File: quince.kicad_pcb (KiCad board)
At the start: 2 copper layers, 70.7 x 53.3 mm, 26 parts, among them J1 NEIGHBOR1, J2 NEIGHBOR2, J7 BONUS_ROW, P9 BASEBAND, U1 TLV3502

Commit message: complete layout
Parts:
- removed P9: BASEBAND, gsg-modules:HEADER-2x8
- added C10: 100pF, gsg-modules:0402, F.Cu at (155.6, 91.8)
- added C11: 100nF, gsg-modules:0402, F.Cu at (151.8, 91.3)
- added C12: 100nF, gsg-modules:0402, F.Cu at (158.7, 87.3)
- added C13: 100nF, gsg-modules:0402, F.Cu at (158.3, 90.2)
- added C14: 100pF, gsg-modules:0402, F.Cu at (145.6, 87.8)
- added C15: 100pF, gsg-modules:0402, F.Cu at (145.6, 85.7)
- added C16: 100pF, gsg-modules:0402, F.Cu at (143.9, 86.2)
- added C17: 100pF, gsg-modules:0402, F.Cu at (143.9, 87.3)
- added C18: 270pF, gsg-modules:0402, F.Cu at (139.7, 83.5)
- added C19: 100nF, gsg-modules:0402, F.Cu at (158.7, 86.2)
- added C2: 1nF, gsg-modules:0402, F.Cu at (158.3, 93.8)
- added C20: 100nF, gsg-modules:0402, F.Cu at (156.8, 82.2)
- added C21: 18pF, gsg-modules:0402, F.Cu at (150.8, 80.8)
- added C22: 68pF, gsg-modules:0402, F.Cu at (149.8, 80.8)
- added C23: 68pF, gsg-modules:0402, F.Cu at (148.8, 80.8)
- added C24: 18pF, gsg-modules:0402, F.Cu at (146.8, 80.8)
- added C25: 100nF, gsg-modules:0402, F.Cu at (141.8, 89.5)
- added C26: 8.2nF, gsg-modules:0402, F.Cu at (141.2, 92.0)
- added C27: 100nF, gsg-modules:0402, F.Cu at (141.3, 84.5)
- added C28: 560pF, gsg-modules:0402, F.Cu at (141.2, 90.8)
- added C29: 10nF, gsg-modules:0402, F.Cu at (136.2, 83.2)
- added C3: 18pF, gsg-modules:0402, F.Cu at (152.2, 93.8)
- added C30: 100nF, gsg-modules:0402, F.Cu at (136.7, 91.5)
- added C31: 100nF, gsg-modules:0402, F.Cu at (157.2, 92.2)
- added C32: 100pF, gsg-modules:0402, F.Cu at (157.2, 91.2)
- added C33: 100nF, gsg-modules:0402, F.Cu at (145.2, 90.0)
- added C34: 100pF, gsg-modules:0402, F.Cu at (146.8, 90.0)
- added C35: 100nF, gsg-modules:0402, F.Cu at (153.8, 80.7)
- added C36: 100pF, gsg-modules:0402, F.Cu at (152.8, 81.8)
- added C37: 10uF, gsg-modules:0805, F.Cu at (133.2, 85.1)
- added C38: C, gsg-modules:0402, F.Cu at (131.4, 87.8)
- added C39: 1nF, gsg-modules:0402, F.Cu at (131.4, 91.8)
- added C4: 68pF, gsg-modules:0402, F.Cu at (151.2, 93.8)
- added C40: 1nF, gsg-modules:0402, F.Cu at (131.4, 89.8)
- added C41: 100nF, gsg-modules:0402, F.Cu at (130.2, 97.2)
- added C42: C, gsg-modules:0402, F.Cu at (131.4, 88.8)
- added C5: 68pF, gsg-modules:0402, F.Cu at (150.2, 93.8)
- added C6: 18pF, gsg-modules:0402, F.Cu at (148.2, 93.8)
- added C7: 1nF, gsg-modules:0402, F.Cu at (164.2, 95.2)
- added C8: 100pF, gsg-modules:0402, F.Cu at (154.6, 91.8)
- added C9: 100pF, gsg-modules:0402, F.Cu at (170.6, 95.2)
- added D1: D_TVS, gsg-modules:0402, F.Cu at (172.2, 94.7)
- added FB1: Ferrite_Bead, gsg-modules:0805, F.Cu at (121.5, 113.0)
- added J10: Conn_01x01, gsg-modules:TESTPOINT-50MIL, F.Cu at (146.6, 97.8)
- added J11: Conn_01x01, gsg-modules:TESTPOINT-50MIL, F.Cu at (143.3, 79.3)
- added J12: Conn_01x01, gsg-modules:TESTPOINT-50MIL, F.Cu at (158.4, 88.8)
- added J13: Conn_01x01, gsg-modules:TESTPOINT-50MIL, F.Cu at (158.4, 84.7)
- added J14: Conn_01x01, gsg-modules:TESTPOINT-50MIL, F.Cu at (160.7, 82.8)
- added J15: Conn_01x01, gsg-modules:TESTPOINT-50MIL, F.Cu at (119.2, 111.8)
- added J16: Conn_01x01, gsg-modules:TESTPOINT-50MIL, F.Cu at (134.7, 90.8)
- added J17: Conn_01x01, gsg-modules:TESTPOINT-50MIL, F.Cu at (122.0, 79.7)
- added J18: Conn_01x01, gsg-modules:TESTPOINT-50MIL, F.Cu at (137.1, 92.8)
- added J19: GND, gsg-modules:HEADER-1x2, F.Cu at (161.4, 103.3)
- added J20: Conn_01x01, gsg-modules:TESTPOINT-50MIL, F.Cu at (133.3, 88.0)
- added J21: Conn_01x01, gsg-modules:TESTPOINT-50MIL, F.Cu at (141.1, 82.5)
- added J3: RFIN, gsg-modules:SMA-EDGE, F.Cu at (177.6, 95.2)
- added J4: Conn_01x01, gsg-modules:TESTPOINT-50MIL, F.Cu at (149.2, 96.8)
- added J5: Conn_01x01, gsg-modules:TESTPOINT-50MIL, B.Cu at (150.8, 86.8)
- added J6: Conn_01x01, gsg-modules:TESTPOINT-50MIL, F.Cu at (157.3, 78.7)
- added J8: LO, gsg-modules:SMA-VERTICAL, F.Cu at (139.6, 98.2)
- added J9: Conn_01x01, gsg-modules:TESTPOINT-50MIL, F.Cu at (155.2, 80.8)
- added L1: 470nH, gsg-modules:0402, F.Cu at (151.7, 95.3)
- added L2: 680nH, gsg-modules:0402, F.Cu at (149.7, 95.3)
- added L3: 470nH, gsg-modules:0402, F.Cu at (149.2, 93.8)
- added L4: 3.6nH, gsg-modules:0402, F.Cu at (162.2, 95.2)
- added L5: 470nH, gsg-modules:0402, F.Cu at (150.3, 79.2)
- added L6: 680nH, gsg-modules:0402, F.Cu at (148.3, 79.2)
- added L7: 470nH, gsg-modules:0402, F.Cu at (147.8, 80.8)
- added R17: 0, gsg-modules:0402, F.Cu at (156.8, 80.5)
- added R18: 0, gsg-modules:0402, F.Cu at (154.7, 82.2)
- added R19: 0, gsg-modules:0402, F.Cu at (151.3, 82.2)
- added R20: 100, gsg-modules:0402, F.Cu at (151.8, 80.8)
- added R21: 0, gsg-modules:0402, F.Cu at (157.9, 80.5)
- added R22: 2k2, gsg-modules:0402, F.Cu at (144.8, 80.8)
- added R23: 10k, gsg-modules:0402, F.Cu at (159.8, 80.0)
- added R24: 51, gsg-modules:0402, F.Cu at (142.3, 85.7)
- added R25: 100, gsg-modules:0402, F.Cu at (145.8, 80.8)
- added R26: 3k3, gsg-modules:0402, F.Cu at (145.3, 79.2)
- added R27: 3k, gsg-modules:0402, F.Cu at (139.7, 91.4)
- added R28: 51, gsg-modules:0402, F.Cu at (142.3, 88.0)
- added R29: 1.5k, gsg-modules:0402, F.Cu at (142.7, 91.5)
- added R30: 0, gsg-modules:0402, F.Cu at (139.1, 93.2)
- added R31: 3k3, gsg-modules:0402, F.Cu at (134.8, 84.2)
- added R32: 0, gsg-modules:0402, F.Cu at (132.8, 99.3)
- added R33: 51, gsg-modules:0402, F.Cu at (131.4, 90.8)
- added U2: AD8347, gsg-modules:TSSOP28, F.Cu at (152.3, 86.8)
- added U3: SAW FILTER, gsg-modules:B9413, F.Cu at (157.2, 95.7)
- added U4: LNA, gsg-modules:BGA7H1N6, F.Cu at (160.1, 95.2)
- added U5: BAND PASS FILTER, gsg-modules:2450BP39D100C, F.Cu at (167.3, 95.2)
- added U6: ADF4360, gsg-modules:QFN24-4, F.Cu at (137.7, 87.5)
- added X1: TCXO, gsg-modules:XTAL5.0x3.2mm, F.Cu at (133.1, 95.7)
- C1: value C -> 100nF; footprint gsg-modules:0603 -> gsg-modules:0402
- R1, R2, R3, R4, R5, R6: footprint gsg-modules:0603 -> gsg-modules:0402
- R10, R16: value R -> 200; footprint gsg-modules:0603 -> gsg-modules:0402
- R11, R7: value R -> 100; footprint gsg-modules:0603 -> gsg-modules:0402
- R12, R13, R14: value R -> 0; footprint gsg-modules:0603 -> gsg-modules:0402
- R15: value R -> 10k; footprint gsg-modules:0603 -> gsg-modules:0402
- R8: value R -> 3k3; footprint gsg-modules:0603 -> gsg-modules:0402
- R9: value R -> 2k2; footprint gsg-modules:0603 -> gsg-modules:0402
- moved R6 46.1 mm to (120.8, 94.9), turned to 90 degrees
- moved R5 44.6 mm to (122.3, 94.9), turned to 90 degrees
- moved R3 39.9 mm to (127.1, 101.6)
- moved R4 39.9 mm to (127.1, 100.1)
- moved U1 31.3 mm to (122.9, 100.8), turned to 270 degrees
- moved R2 26.6 mm to (122.1, 107.7), turned to 90 degrees
- moved R1 24.3 mm to (123.9, 107.7), turned to 90 degrees
- moved C1 24.3 mm to (126.9, 106.3), turned to 180 degrees
- moved R16 24.3 mm to (146.7, 86.8)
- moved R15 23.6 mm to (159.8, 81.2), turned to 0 degrees
- moved R7 19.8 mm to (147.2, 93.8), turned to 270 degrees
- moved R8 18.0 mm to (146.7, 95.3), turned to 0 degrees
- moved R14 16.0 mm to (150.3, 91.8)
- moved R9 15.5 mm to (146.2, 93.8), turned to 90 degrees
- moved R13 12.9 mm to (152.6, 92.3), turned to 0 degrees
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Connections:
- C1 pad 2: VCC -> +3V3
- J1 pad 11: (no net) -> /CLK0
- J1 pad 37: (no net) -> /P1_20
- J1 pad 38: (no net) -> /P1_19
- J1 pad 39: (no net) -> /P1_4
- J2 pad 24: (no net) -> /P3_1
- J2 pad 5: (no net) -> /ADC0_0
- R10 pad 1: /-IN_B -> Net-(C10-Pad2)
- R11 pad 1: VCC -> /IMXO
- R11 pad 2: /+IN_B -> Net-(C3-Pad1)
- R12 pad 1: /+IN_B -> /ENBL
- R12 pad 2: GND -> Net-(R12-Pad2)
- R13 pad 1: VCC -> /IAIN
- R13 pad 2: /-IN_A -> /IMXO
- R14 pad 1: /-IN_A -> /VREF
- R14 pad 2: GND -> /VCMO
- R15 pad 1: VCC -> /ENBL
- R15 pad 2: /+IN_A -> +3V3
- R16 pad 1: /+IN_A -> /LOI_P
- R16 pad 2: GND -> /LOI_N
- R3 pad 1: /+IN_A -> /IN_A+
- R3 pad 2: /RXBBQ- -> /IOP_P
- R4 pad 1: /-IN_A -> /IN_A-
- R4 pad 2: /RXBBQ+ -> /IOP_N
- R5 pad 1: /+IN_B -> /IN_B+
- R5 pad 2: /RXBBI- -> /QOP_N
- R6 pad 1: /-IN_B -> /IN_B-
- R6 pad 2: /RXBBI+ -> /QOP_P
- R7 pad 1: /+IN_A -> /IAIN
- R7 pad 2: /-IN_A -> /VREF
- R8 pad 1: /+IN_B -> /VDT1
- R8 pad 2: /-IN_B -> /VREF
- R9 pad 1: VCC -> /VDT1
- R9 pad 2: /-IN_B -> /IAIN
- U1 pad 1: /+IN_A -> /IN_A-
- U1 pad 2: /-IN_A -> /IN_A+
- U1 pad 3: /+IN_B -> /IN_B+
- U1 pad 4: /-IN_B -> /IN_B-
- U1 pad 8: VCC -> +3V3
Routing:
- net VCC: track 75.7 -> 3.07 mm, vias 4 -> 0
- net GND: track 7.49 -> 74.5 mm, vias 6 -> 42
- net /P1_4: track 0.00 -> 62.7 mm, vias 0 -> 1
- net /P1_20: track 0.00 -> 55.2 mm, vias 0 -> 1
- net /ENBL: track 0.00 -> 52.6 mm, vias 0 -> 2
- net /P1_19: track 0.00 -> 50.6 mm, vias 0 -> 1
- net /VREF: track 0.00 -> 47.7 mm, vias 0 -> 3
- net /QOP_P: track 0.00 -> 38.2 mm
- net +3V3: track 0.00 -> 37.1 mm, vias 0 -> 12
- net /QOP_N: track 0.00 -> 36.7 mm
- net /IOP_P: track 0.00 -> 36.7 mm
- net /CLK0: track 0.00 -> 36.3 mm, vias 0 -> 1
- net /IOP_N: track 0.00 -> 35.9 mm
- net /ADC0_0: track 0.00 -> 34.6 mm
- net /P0_0: track 29.4 -> 9.60 mm
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- added copper zone on In2.Cu, net +3V3
- added copper zone on In1.Cu, net GND
- removed copper zone on B.Cu, net GND
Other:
- copper layers 2 -> 4
- net class Default: clearance 0.1524 -> 0.127
- rule trace_clearance: 0.1524 -> 0.127
- board text added: "+3V3"
- board text added: "3"
- board text added: "3 September 2019"
- board text added: "4"
- board text added: "CE"
- board text added: "ENBL"
- board text added: "IOFS"
- board text added: "LO"
- board text added: "MUXOUT"
- board text added: "QOFS"
- board text added: "REFIN"
- board text added: "VAGC"
- board text added: "VCMO"
- board text added: "VDT1"
- board text added: "VDT2"
- board text added: "VGIN"
- board text added: "VREF"
- board text added: "VTUNE"
- board text removed: "26 January 2019"
- board text removed: "J1: install male pins on other side (do not install stackable header)"
- board text removed: "J2: install male pins on other side (do not install stackable header)"
- board text removed: "J7: do not install"
- board text removed: "install P9 on other side"
- board text removed: "install P9 on this side (male pins)"

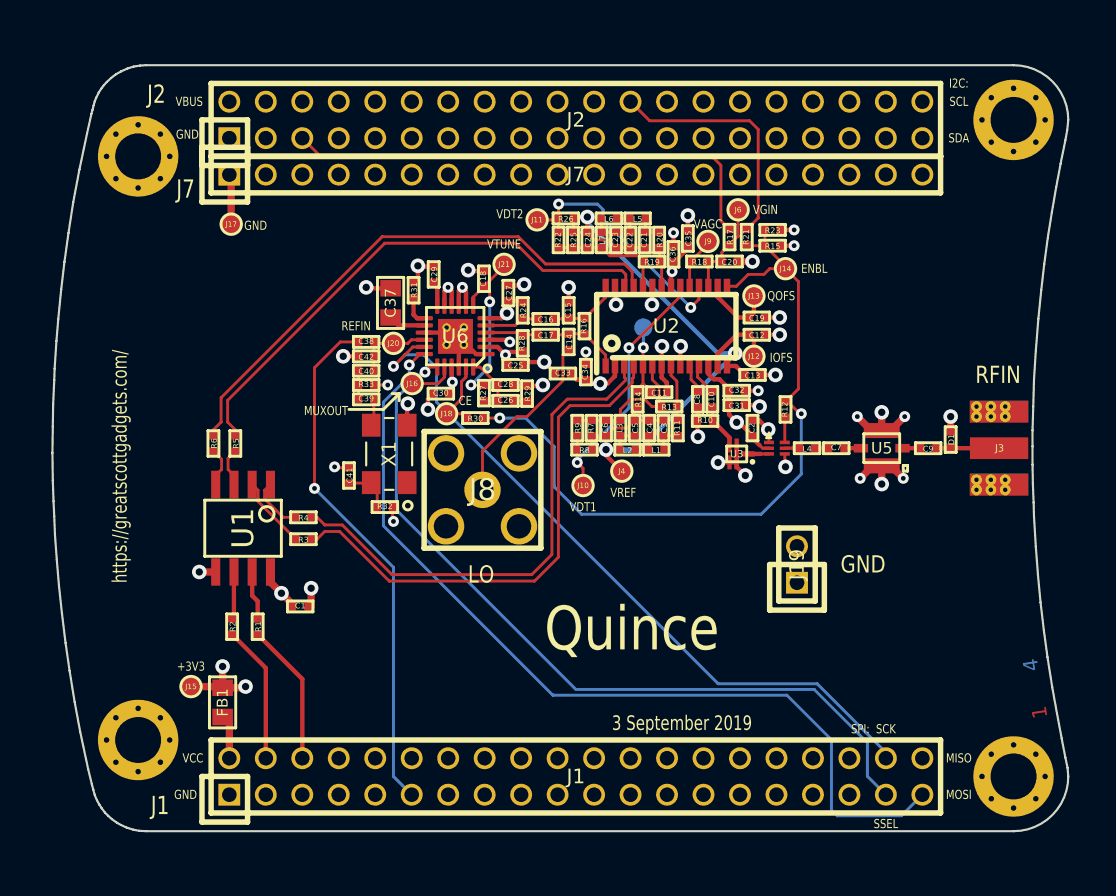
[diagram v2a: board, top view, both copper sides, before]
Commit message: use proper test point symbols
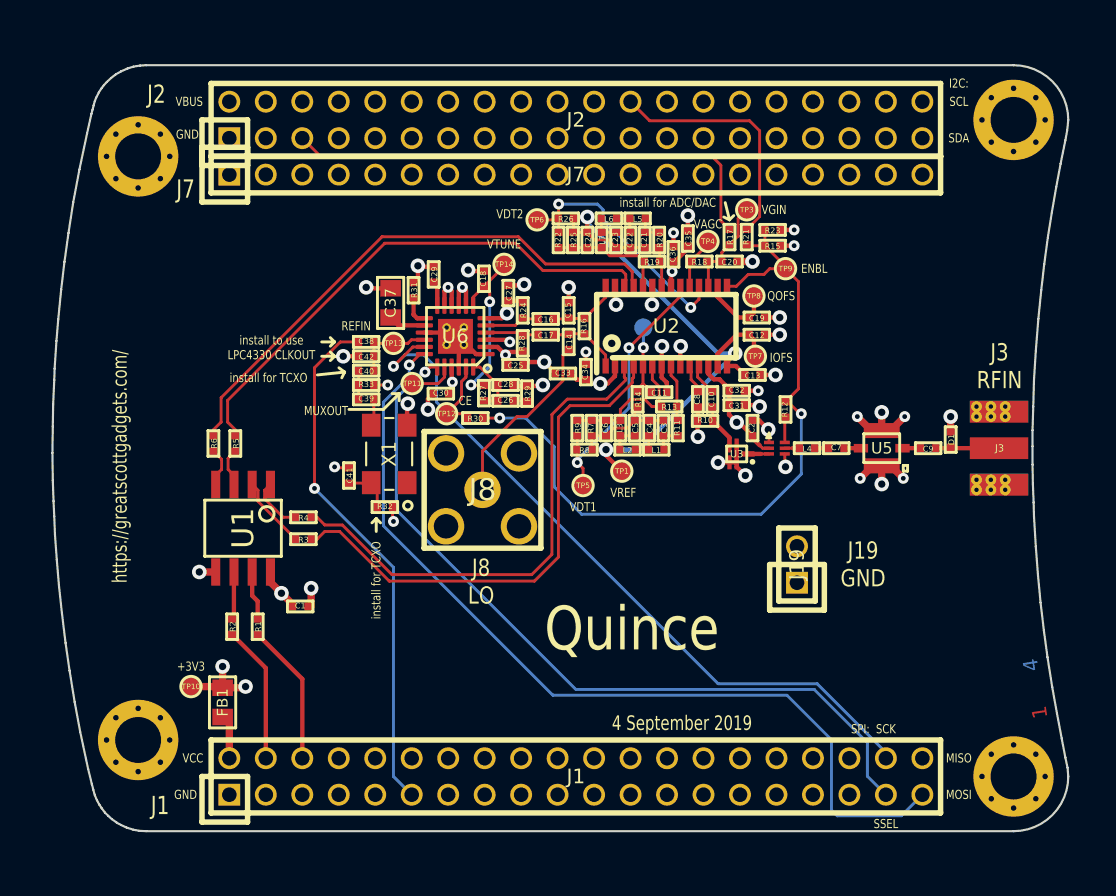
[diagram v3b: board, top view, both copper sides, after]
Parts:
- removed J10, J11, J12, J13, J14, J15, J16, J17, J18, J20, J21, J4, J5, J6, J9: Conn_01x01, gsg-modules:TESTPOINT-50MIL
- added TP1: TestPoint, gsg-modules:TESTPOINT-50MIL, F.Cu at (149.2, 96.8)
- added TP10: TestPoint, gsg-modules:TESTPOINT-50MIL, F.Cu at (119.2, 111.8)
- added TP11: TestPoint, gsg-modules:TESTPOINT-50MIL, F.Cu at (134.7, 90.8)
- added TP12: TestPoint, gsg-modules:TESTPOINT-50MIL, F.Cu at (137.1, 92.8)
- added TP13: TestPoint, gsg-modules:TESTPOINT-50MIL, F.Cu at (133.3, 88.0)
- added TP14: TestPoint, gsg-modules:TESTPOINT-50MIL, F.Cu at (141.1, 82.5)
- added TP2: TestPoint, gsg-modules:TESTPOINT-50MIL, B.Cu at (150.8, 86.8)
- added TP3: TestPoint, gsg-modules:TESTPOINT-50MIL, F.Cu at (157.9, 78.7)
- added TP4: TestPoint, gsg-modules:TESTPOINT-50MIL, F.Cu at (155.2, 80.8)
- added TP5: TestPoint, gsg-modules:TESTPOINT-50MIL, F.Cu at (146.6, 97.8)
- added TP6: TestPoint, gsg-modules:TESTPOINT-50MIL, F.Cu at (143.3, 79.3)
- added TP7: TestPoint, gsg-modules:TESTPOINT-50MIL, F.Cu at (158.6, 88.8)
- added TP8: TestPoint, gsg-modules:TESTPOINT-50MIL, F.Cu at (158.4, 84.7)
- added TP9: TestPoint, gsg-modules:TESTPOINT-50MIL, F.Cu at (160.7, 82.8)
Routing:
- net GND: track 74.5 -> 71.0 mm
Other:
- board text added: "4 September 2019"
- board text added: "J19 GND"
- board text added: "J3 RFIN"
- board text added: "J8 LO"
- board text added: "install for ADC/DAC"
- board text added: "install for TCXO"
- board text added: "install to use LPC4330 CLKOUT"
- board text removed: "3 September 2019"
- board text removed: "LO"

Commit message: assign less confusing names to inner copper layers
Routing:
- added copper zone on C3.Cu, net +3V3
- added copper zone on C2.Cu, net GND
- removed copper zone on In2.Cu, net +3V3
- removed copper zone on In1.Cu, net GND
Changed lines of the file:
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@@
   (layers
     (0 F.Cu signal)
-    (1 In1.Cu signal)
-    (2 In2.Cu signal)
+    (1 C2.Cu signal)
+    (2 C3.Cu signal)
     (31 B.Cu signal)
     (32 B.Adhes user)
@@
     (effects (font (size 1.016 1.016) (thickness 0.1778)))
   )
-  (gr_text 3 (at 177.95 111.45 98.9) (layer In2.Cu)
+  (gr_text 3 (at 177.95 111.45 98.9) (layer C3.Cu)
     (effects (font (size 1.016 1.016) (thickness 0.1778)))
   )
@@
     (effects (font (size 1.016 0.762) (thickness 0.1524)))
   )
-  (gr_text 2 (at 178.181 112.6236 98.9) (layer In1.Cu)
+  (gr_text 2 (at 178.181 112.6236 98.9) (layer C2.Cu)
     (effects (font (size 1.016 1.016) (thickness 0.1778)))
   )
@@
   (segment (start 121.3794 96.0228) (end 120.812 95.4554) (width 0.2032) (layer F.Cu) (net 67))
   (segment (start 121.3794 96.7306) (end 121.3794 96.0228) (width 0.2032) (layer F.Cu) (net 67))
-  (zone (net 1) (net_name GND) (layer In1.Cu) (hatch edge 0.508)
+  (zone (net 1) (net_name GND) (layer C2.Cu) (hatch edge 0.508)
     (connect_pads (clearance 0.254))
     (min_thickness 0.254)
@@
     )
   )
-  (zone (net 7) (net_name +3V3) (layer In2.Cu) (hatch edge 0.508)
+  (zone (net 7) (net_name +3V3) (layer C3.Cu) (hatch edge 0.508)
     (connect_pads (clearance 0.254))
     (min_thickness 0.254)

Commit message: select parts
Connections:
- J1 pad 10: (no net) -> /P1_1
- J1 pad 12: (no net) -> /P1_2
- J1 pad 13: (no net) -> /P1_5
- J1 pad 14: (no net) -> /P5_2
- J1 pad 15: (no net) -> /P1_7
- J1 pad 16: (no net) -> /P1_6
- J1 pad 17: (no net) -> /P1_9
- J1 pad 18: (no net) -> /P1_8
- J1 pad 19: (no net) -> /P5_3
- J1 pad 20: (no net) -> /P1_10
- J1 pad 21: (no net) -> /P1_12
- J1 pad 22: (no net) -> /P1_11
- J1 pad 23: (no net) -> /P5_5
- J1 pad 24: (no net) -> /P5_4
- J1 pad 25: (no net) -> /P1_14
- J1 pad 26: (no net) -> /P1_13
- J1 pad 27: (no net) -> /P5_6
- J1 pad 28: (no net) -> /P1_15
- J1 pad 29: (no net) -> /P5_7
- J1 pad 3: (no net) -> /P4_9
- J1 pad 30: (no net) -> /P1_16
- J1 pad 31: (no net) -> /P1_18
- J1 pad 32: (no net) -> /P1_17
- J1 pad 33: (no net) -> /P9_5
- J1 pad 34: (no net) -> /P9_6
- J1 pad 35: (no net) -> /P2_0
- J1 pad 36: (no net) -> /P6_0
- J1 pad 40: (no net) -> /P1_3
- J1 pad 5: (no net) -> /P4_10
- J1 pad 7: (no net) -> /P1_0
- J1 pad 8: (no net) -> /P5_0
- J1 pad 9: (no net) -> /P5_1
- J2 pad 10: (no net) -> /P4_6
- J2 pad 11: (no net) -> /P4_7
- J2 pad 12: (no net) -> /CLK2
- J2 pad 13: (no net) -> /P2_8
- J2 pad 14: (no net) -> /P2_7
- J2 pad 15: (no net) -> /P2_6
- J2 pad 16: (no net) -> /P7_7
- J2 pad 17: (no net) -> /WAKEUP0
- J2 pad 18: (no net) -> /P2_5
- J2 pad 19: (no net) -> /P2_4
- J2 pad 2: (no net) -> /+5V
- J2 pad 20: (no net) -> /P2_3
- J2 pad 21: (no net) -> /PF_4
- J2 pad 22: (no net) -> /P3_2
- J2 pad 23: (no net) -> /P7_2
- J2 pad 25: (no net) -> /P7_1
- J2 pad 26: (no net) -> /P3_0
- J2 pad 27: (no net) -> /P7_0
- J2 pad 28: (no net) -> /P3_4
- J2 pad 29: (no net) -> /P6_8
- J2 pad 3: (no net) -> /P4_8
- J2 pad 30: (no net) -> /P3_7
- J2 pad 31: (no net) -> /P6_7
- J2 pad 32: (no net) -> /P3_3
- J2 pad 33: (no net) -> /P2_2
- J2 pad 34: (no net) -> /P6_6
- J2 pad 35: (no net) -> /P2_1
- J2 pad 36: (no net) -> /P6_3
- J2 pad 37: (no net) -> /P3_5
- J2 pad 38: (no net) -> /P3_6
- J2 pad 39: (no net) -> /I2C0_SDA
- J2 pad 4: (no net) -> /P4_0
- J2 pad 40: (no net) -> /I2C0_SCL
- J2 pad 6: (no net) -> /P4_5
- J2 pad 7: (no net) -> /P4_4
- J2 pad 8: (no net) -> /P4_2
- J2 pad 9: (no net) -> /P4_3
- J7 pad 11: (no net) -> /RESET
- J7 pad 12: (no net) -> /VBAT
- J7 pad 13: (no net) -> /P2_11
- J7 pad 14: (no net) -> /P2_10
- J7 pad 15: (no net) -> /P6_10
- J7 pad 16: (no net) -> /P6_9
- J7 pad 17: (no net) -> /P6_2
- J7 pad 18: (no net) -> /P6_1
- J7 pad 2: (no net) -> /P6_4
- J7 pad 20: (no net) -> Net-(J7-Pad20)
- J7 pad 3: (no net) -> /P6_5
- J7 pad 4: (no net) -> /ADC0_5
- J7 pad 5: (no net) -> /ADC0_2
- J7 pad 6: (no net) -> /P2_9
- J7 pad 7: (no net) -> /P2_12
- J7 pad 8: (no net) -> /P2_13
- J7 pad 9: (no net) -> /RTC_ALARM
- X1 pad 1: (no net) -> Net-(X1-Pad1)

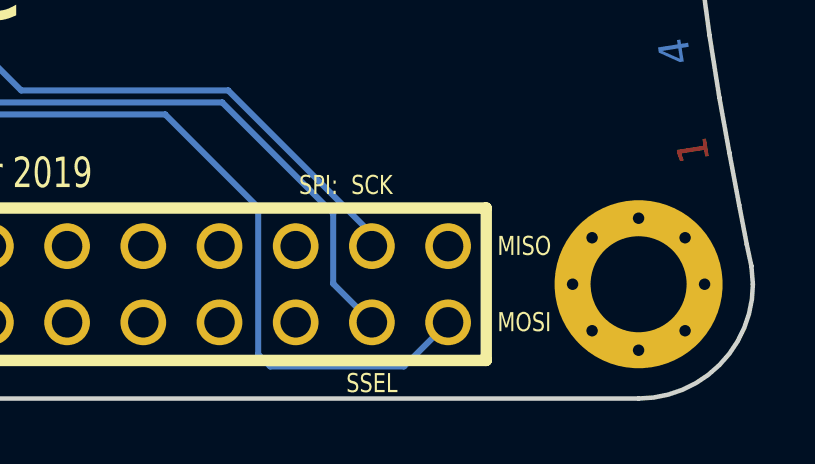
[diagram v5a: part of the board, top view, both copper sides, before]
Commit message: adopt OSHWA convention for SPI signal names https://www.oshwa.org/a-resolution-to-redefine-spi-signal-names
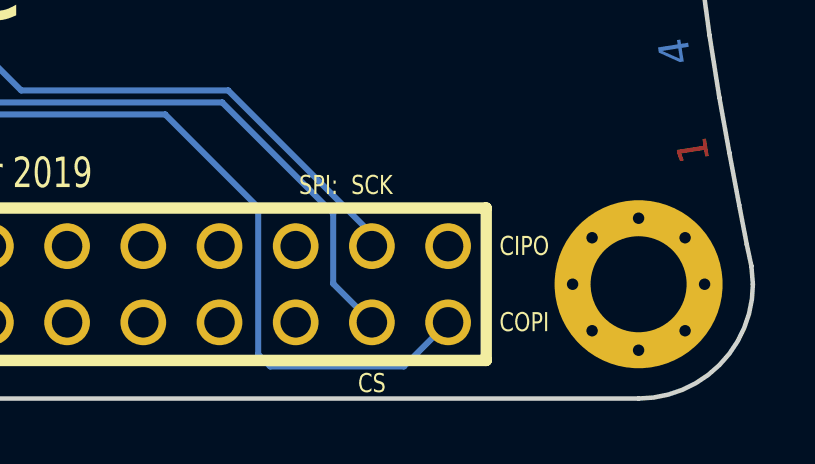
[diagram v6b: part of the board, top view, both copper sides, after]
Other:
- board text added: "CIPO"
- board text added: "COPI"
- board text added: "CS"
- board text removed: "MISO"
- board text removed: "MOSI"
- board text removed: "SSEL"
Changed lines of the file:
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@@
     (effects (font (size 0.635 0.508) (thickness 0.1016)))
   )
-  (gr_text SSEL (at 167.64 121.412) (layer F.SilkS)
+  (gr_text CS (at 167.64 121.412) (layer F.SilkS)
     (effects (font (size 0.635 0.508) (thickness 0.1016)))
   )
-  (gr_text MISO (at 172.72 116.84) (layer F.SilkS)
+  (gr_text CIPO (at 172.72 116.84) (layer F.SilkS)
     (effects (font (size 0.635 0.508) (thickness 0.1016)))
   )
-  (gr_text MOSI (at 172.72 119.38) (layer F.SilkS)
+  (gr_text COPI (at 172.72 119.38) (layer F.SilkS)
     (effects (font (size 0.635 0.508) (thickness 0.1016)))
   )
